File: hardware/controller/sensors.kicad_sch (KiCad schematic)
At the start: 9 parts, among them U7 PMW3901, U8 MPU-6050

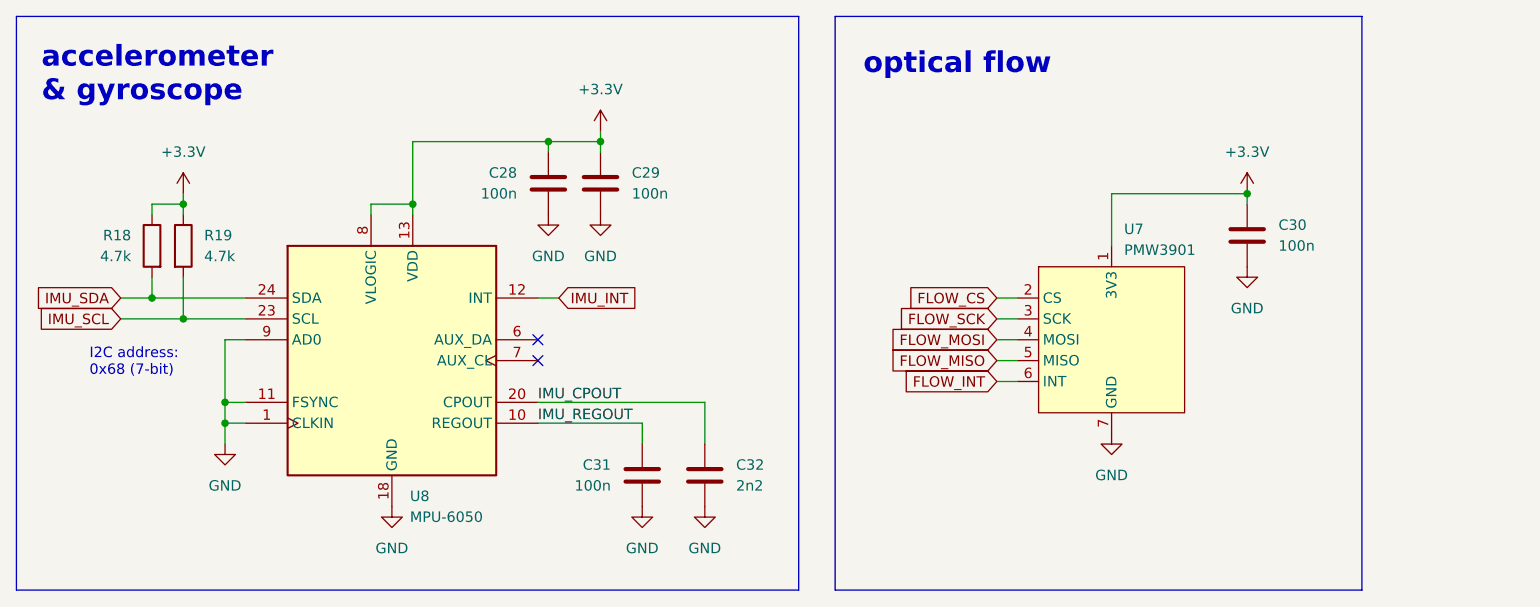
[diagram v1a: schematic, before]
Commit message: change P-MOSFET on the battery enter
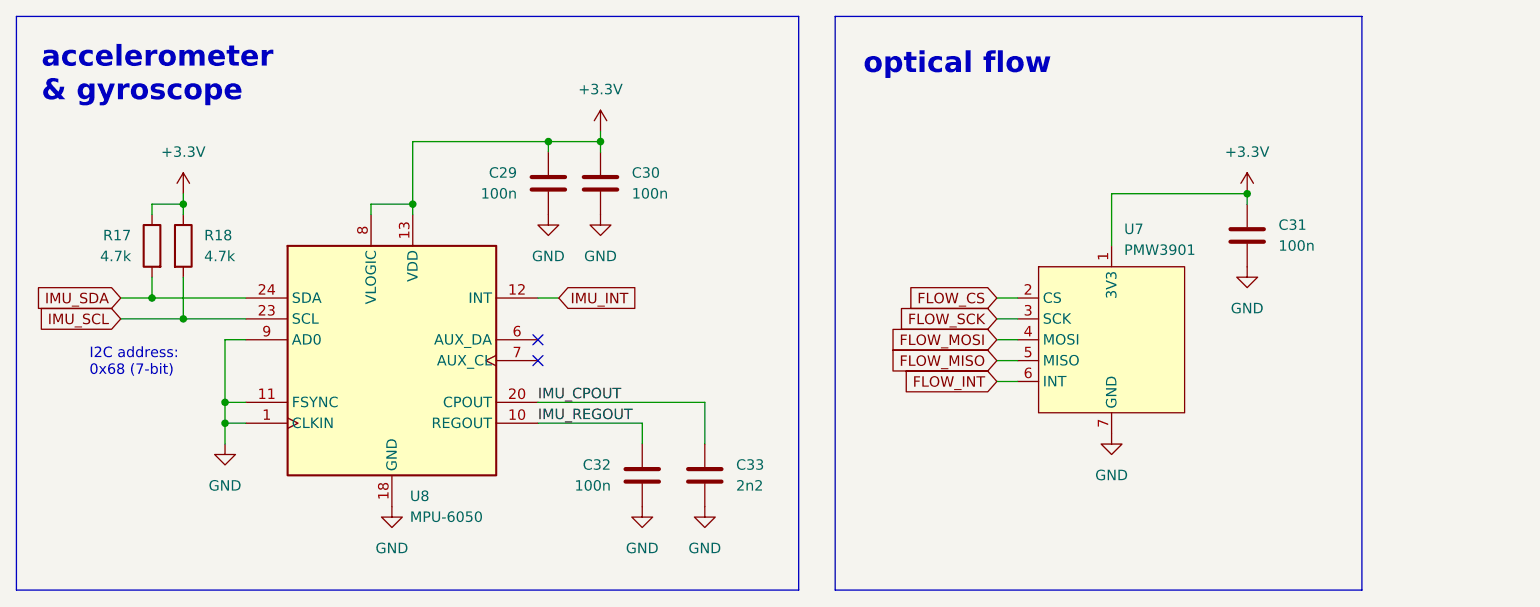
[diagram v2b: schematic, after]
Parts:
- renumbered C28 to C29, C29 to C30, C30 to C31, C31 to C32, C32 to C33, R18 to R17, R19 to R18
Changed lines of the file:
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@@
 		(dnp no)
 		(fields_autoplaced yes)
-		(property "Reference" "C28"
+		(property "Reference" "C29"
 			(at 101.6 69.8499 0)
 			(effects
@@
 			(project "controller"
 				(path "/b81e4285-7ba7-4843-ab37-49bb8c6c135f/9b959a7f-7785-4fbc-97ae-e71bdac42a24"
-					(reference "C28")
+					(reference "C29")
 					(unit 1)
 				)
@@
 		(on_board yes)
 		(dnp no)
-		(property "Reference" "C31"
+		(property "Reference" "C32"
 			(at 113.03 105.4099 0)
 			(effects
@@
 			(project "controller"
 				(path "/b81e4285-7ba7-4843-ab37-49bb8c6c135f/9b959a7f-7785-4fbc-97ae-e71bdac42a24"
-					(reference "C31")
+					(reference "C32")
 					(unit 1)
 				)
@@
 		(dnp no)
 		(fields_autoplaced yes)
-		(property "Reference" "R19"
+		(property "Reference" "R18"
 			(at 63.5 77.4699 0)
 			(effects
@@
 			(project "controller"
 				(path "/b81e4285-7ba7-4843-ab37-49bb8c6c135f/9b959a7f-7785-4fbc-97ae-e71bdac42a24"
-					(reference "R19")
+					(reference "R18")
 					(unit 1)
 				)
@@
 		(dnp no)
 		(fields_autoplaced yes)
-		(property "Reference" "C29"
+		(property "Reference" "C30"
 			(at 115.57 69.8499 0)
 			(effects
@@
 			(project "controller"
 				(path "/b81e4285-7ba7-4843-ab37-49bb8c6c135f/9b959a7f-7785-4fbc-97ae-e71bdac42a24"
-					(reference "C29")
+					(reference "C30")
 					(unit 1)
 				)
@@
 		(dnp no)
 		(fields_autoplaced yes)
-		(property "Reference" "C30"
+		(property "Reference" "C31"
 			(at 194.31 76.1999 0)
 			(effects
@@
 			(project "controller"
 				(path "/b81e4285-7ba7-4843-ab37-49bb8c6c135f/9b959a7f-7785-4fbc-97ae-e71bdac42a24"
-					(reference "C30")
+					(reference "C31")
 					(unit 1)
 				)
@@
 		(dnp no)
 		(fields_autoplaced yes)
-		(property "Reference" "C32"
+		(property "Reference" "C33"
 			(at 128.27 105.4099 0)
 			(effects
@@
 			(project "controller"
 				(path "/b81e4285-7ba7-4843-ab37-49bb8c6c135f/9b959a7f-7785-4fbc-97ae-e71bdac42a24"
-					(reference "C32")
+					(reference "C33")
 					(unit 1)
 				)
@@
 		(on_board yes)
 		(dnp no)
-		(property "Reference" "R18"
+		(property "Reference" "R17"
 			(at 54.61 77.4699 0)
 			(effects
@@
 			(project "controller"
 				(path "/b81e4285-7ba7-4843-ab37-49bb8c6c135f/9b959a7f-7785-4fbc-97ae-e71bdac42a24"
-					(reference "R18")
-					(unit 1)
-				)
+					(reference "R17")
+					(unit 1)
+				)

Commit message: footprints, layout
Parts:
- removed U7: PMW3901, symbol hogger2:PMW3901
- added C32: 10u, Capacitor_SMD:C_0603_1608Metric, symbol Device:C
- added J4: Conn_01x07, Connector_PinHeader_2.54mm:PinHeader_1x07_P2.54mm_Horizontal, symbol Connector_Generic:Conn_01x07
- renumbered C29 to C30, C30 to C31, C31 to C33, C32 to C34, C33 to C35, U8 to U7
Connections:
- net +3.3V: now also C32.1, J4.1 (Pin_1)
- net FLOW_CS: now also J4.2 (Pin_2)
- net FLOW_INT: now also J4.6 (Pin_6)
- net FLOW_MISO: now also J4.5 (Pin_5)
- net FLOW_MOSI: now also J4.4 (Pin_4)
- net FLOW_SCK: now also J4.3 (Pin_3)
- net GND: now also C32.2, J4.7 (Pin_7)
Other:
- note added: "connected to external PMW3901 dev-board"
- moved on the sheet: C33

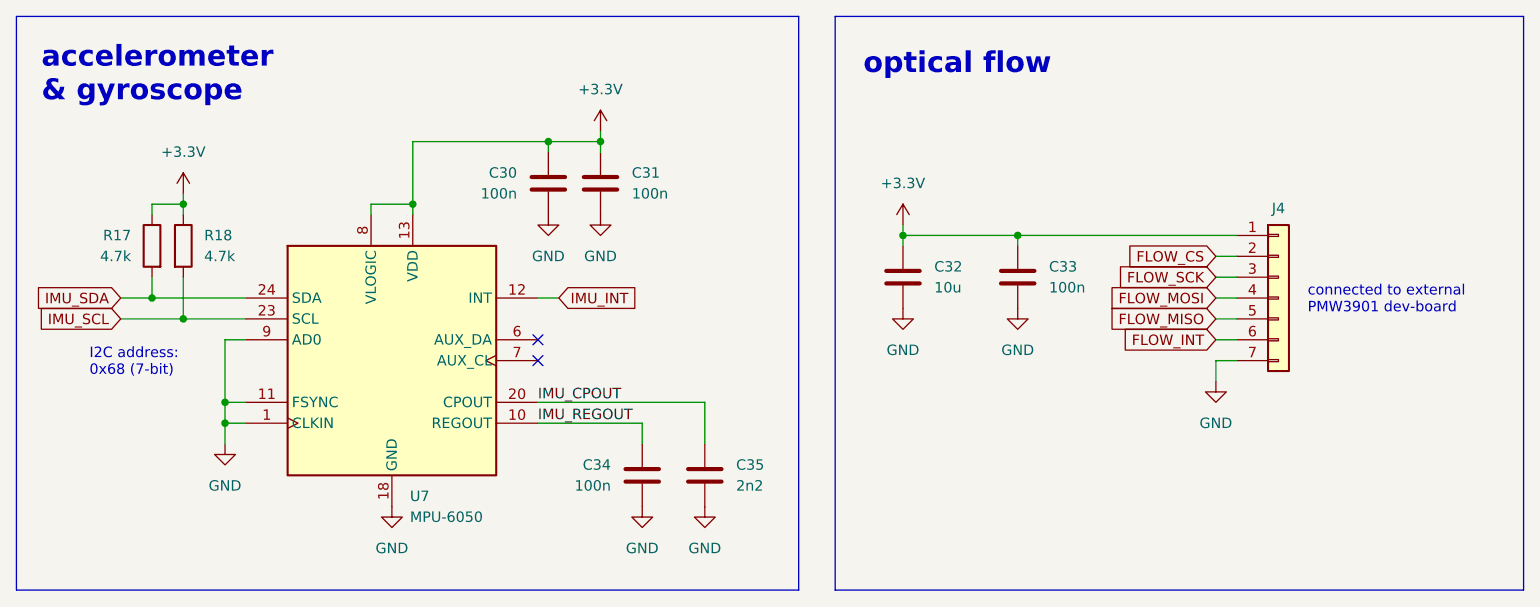
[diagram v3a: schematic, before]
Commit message: add VBUS sense to STM and ESP, change buttons and sw to vertical, add USB-C to SEM
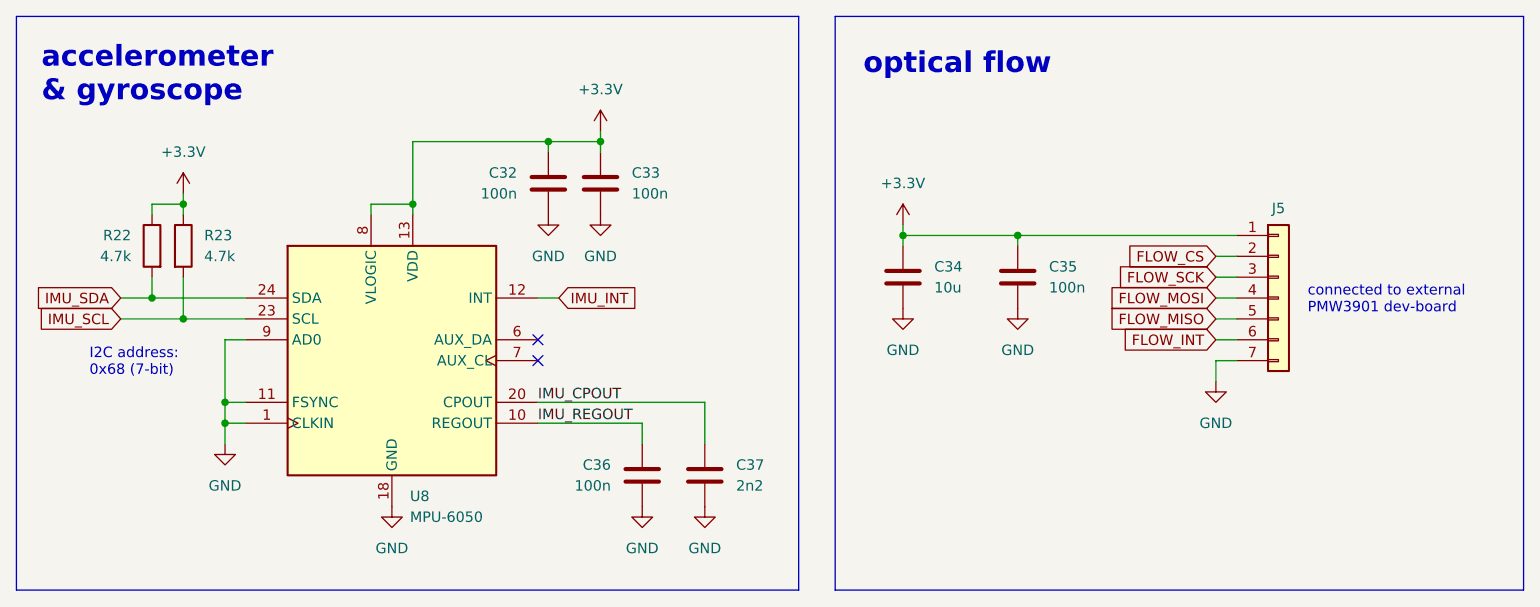
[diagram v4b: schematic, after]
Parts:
- renumbered C30 to C32, C31 to C33, C32 to C34, C33 to C35, C34 to C36, C35 to C37, J4 to J5, R17 to R22, R18 to R23, U7 to U8

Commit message: custom footprints with all 3D models
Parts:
- U8: footprint Sensor_Motion:InvenSense_QFN-24_4x4mm_P0.5mm -> hogger2:MPU6050_handsolder
- renumbered C32 to C30, C33 to C31, C34 to C32, C35 to C33, C36 to C34, C37 to C35
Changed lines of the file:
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@@
 		(dnp no)
 		(fields_autoplaced yes)
-		(property "Reference" "#PWR075"
+		(property "Reference" "#PWR073"
 			(at 111.76 68.58 0)
 			(effects
@@
 			(project "controller"
 				(path "/b81e4285-7ba7-4843-ab37-49bb8c6c135f/9b959a7f-7785-4fbc-97ae-e71bdac42a24"
-					(reference "#PWR075")
+					(reference "#PWR073")
 					(unit 1)
 				)
@@
 			)
 		)
-		(property "Footprint" "Sensor_Motion:InvenSense_QFN-24_4x4mm_P0.5mm"
+		(property "Footprint" "hogger2:MPU6050_handsolder"
 			(at 86.36 113.03 0)
 			(effects
@@
 		(dnp no)
 		(fields_autoplaced yes)
-		(property "Reference" "C32"
+		(property "Reference" "C30"
 			(at 101.6 69.8499 0)
 			(effects
@@
 			(project "controller"
 				(path "/b81e4285-7ba7-4843-ab37-49bb8c6c135f/9b959a7f-7785-4fbc-97ae-e71bdac42a24"
-					(reference "C32")
+					(reference "C30")
 					(unit 1)
 				)
@@
 		(on_board yes)
 		(dnp no)
-		(property "Reference" "C36"
+		(property "Reference" "C34"
 			(at 113.03 105.4099 0)
 			(effects
@@
 			(project "controller"
 				(path "/b81e4285-7ba7-4843-ab37-49bb8c6c135f/9b959a7f-7785-4fbc-97ae-e71bdac42a24"
-					(reference "C36")
+					(reference "C34")
 					(unit 1)
 				)
@@
 		(dnp no)
 		(fields_autoplaced yes)
-		(property "Reference" "#PWR085"
+		(property "Reference" "#PWR083"
 			(at 116.84 116.84 0)
 			(effects
@@
 			(project "controller"
 				(path "/b81e4285-7ba7-4843-ab37-49bb8c6c135f/9b959a7f-7785-4fbc-97ae-e71bdac42a24"
-					(reference "#PWR085")
+					(reference "#PWR083")
 					(unit 1)
 				)
@@
 		(on_board yes)
 		(dnp no)
-		(property "Reference" "C34"
+		(property "Reference" "C32"
 			(at 152.4 81.2799 0)
 			(effects
@@
 			(project "controller"
 				(path "/b81e4285-7ba7-4843-ab37-49bb8c6c135f/9b959a7f-7785-4fbc-97ae-e71bdac42a24"
-					(reference "C34")
+					(reference "C32")
 					(unit 1)
 				)
@@
 		(dnp no)
 		(fields_autoplaced yes)
-		(property "Reference" "#PWR082"
+		(property "Reference" "#PWR080"
 			(at 186.69 101.6 0)
 			(effects
@@
 			(project "controller"
 				(path "/b81e4285-7ba7-4843-ab37-49bb8c6c135f/9b959a7f-7785-4fbc-97ae-e71bdac42a24"
-					(reference "#PWR082")
+					(reference "#PWR080")
 					(unit 1)
 				)
@@
 		(dnp no)
 		(fields_autoplaced yes)
-		(property "Reference" "C33"
+		(property "Reference" "C31"
 			(at 115.57 69.8499 0)
 			(effects
@@
 			(project "controller"
 				(path "/b81e4285-7ba7-4843-ab37-49bb8c6c135f/9b959a7f-7785-4fbc-97ae-e71bdac42a24"
-					(reference "C33")
+					(reference "C31")
 					(unit 1)
 				)
@@
 		(dnp no)
 		(fields_autoplaced yes)
-		(property "Reference" "#PWR081"
+		(property "Reference" "#PWR079"
 			(at 162.56 92.71 0)
 			(effects
@@
 			(project "controller"
 				(path "/b81e4285-7ba7-4843-ab37-49bb8c6c135f/9b959a7f-7785-4fbc-97ae-e71bdac42a24"
-					(reference "#PWR081")
+					(reference "#PWR079")
 					(unit 1)
 				)
@@
 		(dnp no)
 		(fields_autoplaced yes)
-		(property "Reference" "#PWR076"
+		(property "Reference" "#PWR074"
 			(at 60.96 76.2 0)
 			(effects
@@
 			(project "controller"
 				(path "/b81e4285-7ba7-4843-ab37-49bb8c6c135f/9b959a7f-7785-4fbc-97ae-e71bdac42a24"
-					(reference "#PWR076")
+					(reference "#PWR074")
 					(unit 1)
 				)
@@
 		(on_board yes)
 		(dnp no)
-		(property "Reference" "C35"
+		(property "Reference" "C33"
 			(at 166.37 81.2799 0)
 			(effects
@@
 			(project "controller"
 				(path "/b81e4285-7ba7-4843-ab37-49bb8c6c135f/9b959a7f-7785-4fbc-97ae-e71bdac42a24"
-					(reference "C35")
+					(reference "C33")
 					(unit 1)
 				)
@@
 		(dnp no)
 		(fields_autoplaced yes)
-		(property "Reference" "#PWR077"
+		(property "Reference" "#PWR075"
 			(at 105.41 81.28 0)
 			(effects
@@
 			(project "controller"
 				(path "/b81e4285-7ba7-4843-ab37-49bb8c6c135f/9b959a7f-7785-4fbc-97ae-e71bdac42a24"
-					(reference "#PWR077")
+					(reference "#PWR075")
 					(unit 1)
 				)
@@
 		(dnp no)
 		(fields_autoplaced yes)
-		(property "Reference" "C37"
+		(property "Reference" "C35"
 			(at 128.27 105.4099 0)
 			(effects
@@
 			(project "controller"
 				(path "/b81e4285-7ba7-4843-ab37-49bb8c6c135f/9b959a7f-7785-4fbc-97ae-e71bdac42a24"
-					(reference "C37")
+					(reference "C35")
 					(unit 1)
 				)
@@
 		(dnp no)
 		(fields_autoplaced yes)
-		(property "Reference" "#PWR084"
+		(property "Reference" "#PWR082"
 			(at 86.36 116.84 0)
 			(effects
@@
 			(project "controller"
 				(path "/b81e4285-7ba7-4843-ab37-49bb8c6c135f/9b959a7f-7785-4fbc-97ae-e71bdac42a24"
-					(reference "#PWR084")
+					(reference "#PWR082")
 					(unit 1)
 				)
@@
 		(dnp no)
 		(fields_autoplaced yes)
-		(property "Reference" "#PWR083"
+		(property "Reference" "#PWR081"
 			(at 66.04 109.22 0)
 			(effects
@@
 			(project "controller"
 				(path "/b81e4285-7ba7-4843-ab37-49bb8c6c135f/9b959a7f-7785-4fbc-97ae-e71bdac42a24"
-					(reference "#PWR083")
+					(reference "#PWR081")
 					(unit 1)
 				)
@@
 		(dnp no)
 		(fields_autoplaced yes)
-		(property "Reference" "#PWR078"
+		(property "Reference" "#PWR076"
 			(at 111.76 81.28 0)
 			(effects
@@
 			(project "controller"
 				(path "/b81e4285-7ba7-4843-ab37-49bb8c6c135f/9b959a7f-7785-4fbc-97ae-e71bdac42a24"
-					(reference "#PWR078")
+					(reference "#PWR076")
 					(unit 1)
 				)
@@
 		(dnp no)
 		(fields_autoplaced yes)
-		(property "Reference" "#PWR080"
+		(property "Reference" "#PWR078"
 			(at 148.59 92.71 0)
 			(effects
@@
 			(project "controller"
 				(path "/b81e4285-7ba7-4843-ab37-49bb8c6c135f/9b959a7f-7785-4fbc-97ae-e71bdac42a24"
-					(reference "#PWR080")
+					(reference "#PWR078")
 					(unit 1)
 				)
@@
 		(dnp no)
 		(fields_autoplaced yes)
-		(property "Reference" "#PWR079"
+		(property "Reference" "#PWR077"
 			(at 148.59 80.01 0)
 			(effects
@@
 			(project "controller"
 				(path "/b81e4285-7ba7-4843-ab37-49bb8c6c135f/9b959a7f-7785-4fbc-97ae-e71bdac42a24"
-					(reference "#PWR079")
+					(reference "#PWR077")
 					(unit 1)
 				)
@@
 		(dnp no)
 		(fields_autoplaced yes)
-		(property "Reference" "#PWR086"
+		(property "Reference" "#PWR084"
 			(at 124.46 116.84 0)
 			(effects
@@
 			(project "controller"
 				(path "/b81e4285-7ba7-4843-ab37-49bb8c6c135f/9b959a7f-7785-4fbc-97ae-e71bdac42a24"
-					(reference "#PWR086")
-					(unit 1)
-				)
+					(reference "#PWR084")
+					(unit 1)
+				)
